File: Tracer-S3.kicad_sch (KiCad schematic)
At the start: 41 parts, among them J1 Conn_01x06_Socket, J2 Conn_02x02_Odd_Even, J3 Conn_02x02_Odd_Even, J4 Conn_02x02_Odd_Even, J5 Conn_02x02_Odd_Even, J6 Conn_02x04_Odd_Even, J7 Conn_01x02_Pin, Q1 BSP89, SW1 SW_Push, SW2 SW_Push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

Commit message: v2
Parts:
- added D4: D_Schottky, Diode_SMD:D_SOD-123, symbol Device:D_Schottky
- R1, R12, R13, R14, R15: LCSC C3017715 -> C269701
- R10, R11, R6, R8, R9: value R -> 33k; footprint Resistor_THT:R_Axial_DIN0204_L3.6mm_D1.6mm_P7.62mm_Horizontal -> Resistor_THT:R_Axial_DIN0207_L6.3mm_D2.5mm_P10.16mm_Horizontal
- R2, R3, R4, R5, R7: value R -> 47R; footprint Resistor_THT:R_Axial_DIN0204_L3.6mm_D1.6mm_P7.62mm_Horizontal -> Resistor_THT:R_Axial_DIN0207_L6.3mm_D2.5mm_P10.16mm_Horizontal
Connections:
- net +BATT: now also D4.1 (K); no longer SW3.1 (A)
- net FET_GATE: now reaches U1.12 (GPIO8/TOUCH8/ADC1_CH7/SUBSPICS1)
- net FET_GATE: now also Q1.1 (G)
- new net: D4.2 (A), SW3.1 (A)

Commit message: 部品定数修正
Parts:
- renumbered R7 to R6, R6 to R7
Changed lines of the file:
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@@
   (symbol (lib_id "Device:R") (at 210.82 69.85 90) (unit 1)
     (in_bom yes) (on_board yes) (dnp no) (fields_autoplaced)
-    (property "Reference" "R7" (at 210.82 63.5 90)
+    (property "Reference" "R6" (at 210.82 63.5 90)
       (effects (font (size 1.27 1.27)))
     )
@@
       (project "Tracer-S3"
         (path "/54f48c7a-ecf4-411c-a572-7361fca9981f"
-          (reference "R7") (unit 1)
+          (reference "R6") (unit 1)
         )
       )
@@
   (symbol (lib_id "Device:R") (at 170.18 41.91 90) (unit 1)
     (in_bom yes) (on_board yes) (dnp no) (fields_autoplaced)
-    (property "Reference" "R6" (at 170.18 35.56 90)
+    (property "Reference" "R7" (at 170.18 35.56 90)
       (effects (font (size 1.27 1.27)))
     )
@@
       (project "Tracer-S3"
         (path "/54f48c7a-ecf4-411c-a572-7361fca9981f"
-          (reference "R6") (unit 1)
+          (reference "R7") (unit 1)
         )
       )

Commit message: 回路定数変更
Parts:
- R10, R11, R7, R8, R9: value 33k -> 10k
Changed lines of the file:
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@@
       (effects (font (size 1.27 1.27)))
     )
-    (property "Value" "33k" (at 170.18 71.12 90)
+    (property "Value" "10k" (at 170.18 71.12 90)
       (effects (font (size 1.27 1.27)))
     )
@@
       (effects (font (size 1.27 1.27)))
     )
-    (property "Value" "33k" (at 233.68 58.42 90)
+    (property "Value" "10k" (at 233.68 58.42 90)
       (effects (font (size 1.27 1.27)))
     )
@@
       (effects (font (size 1.27 1.27)))
     )
-    (property "Value" "33k" (at 170.18 38.1 90)
+    (property "Value" "10k" (at 170.18 38.1 90)
       (effects (font (size 1.27 1.27)))
     )
@@
       (effects (font (size 1.27 1.27)))
     )
-    (property "Value" "33k" (at 233.68 43.18 90)
+    (property "Value" "10k" (at 233.68 43.18 90)
       (effects (font (size 1.27 1.27)))
     )
@@
       (effects (font (size 1.27 1.27)))
     )
-    (property "Value" "33k" (at 233.68 27.94 90)
-      (effects (font (size 1.27 1.27)))
-    )
+    (property "Value" "10k" (at 233.68 27.94 90)
+      (effects (font (size 1.27 1.27)))
+    )

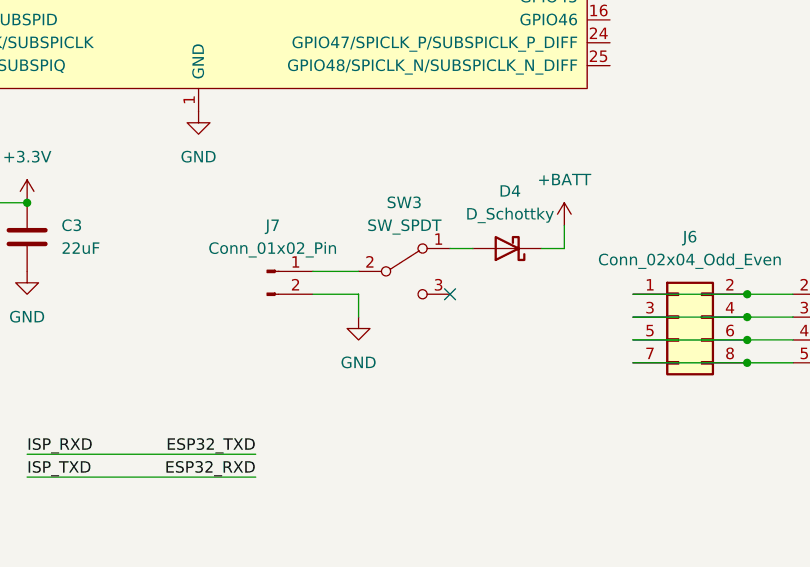
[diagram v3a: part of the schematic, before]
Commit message: 電源スイッチ配線変更・ミシン穴追加
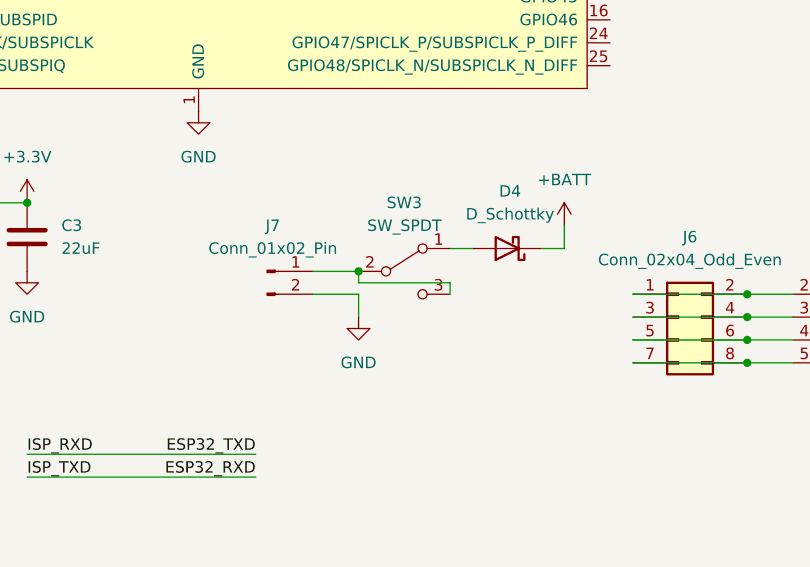
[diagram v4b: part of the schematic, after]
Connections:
- net at J7.1 (Pin_1), SW3.2 (B): now also SW3.3 (C)
- no-connect marks 3 -> 2
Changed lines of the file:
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@@
   (junction (at 227.33 62.23) (diameter 0) (color 0 0 0 0)
   )
+  (junction (at 100.33 134.62) (diameter 0) (color 0 0 0 0)
+  )
   (junction (at 143.51 142.24) (diameter 0) (color 0 0 0 0)
   )
@@
   )
   (no_connect (at 36.83 48.26))
-  (no_connect (at 110.49 137.16))
   (no_connect (at 128.27 66.04))
   (wire (pts (xy 128.27 93.98) (xy 139.7 93.98))
@@
     (stroke (width 0) (type default))
   )
+  (wire (pts (xy 110.49 137.16) (xy 110.49 135.89))
+    (stroke (width 0) (type default))
+  )
   (wire (pts (xy 227.33 46.99) (xy 227.33 62.23))
     (stroke (width 0) (type default))
@@
     (stroke (width 0) (type default))
   )
+  (wire (pts (xy 100.33 135.89) (xy 100.33 134.62))
+    (stroke (width 0) (type default))
+  )
   (wire (pts (xy 176.53 36.83) (xy 179.07 36.83))
     (stroke (width 0) (type default))
@@
     (stroke (width 0) (type default))
   )
+  (wire (pts (xy 110.49 135.89) (xy 100.33 135.89))
+    (stroke (width 0) (type default))
+  )
